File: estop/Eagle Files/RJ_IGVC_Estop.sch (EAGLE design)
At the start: 28 parts, among them U1 LD1086D2M33TR, U4 ATMEGA328P-AUR, X1 2X3SHROUDED, X2 1751248, X3 1751248, X4 1751248, X5 1751248

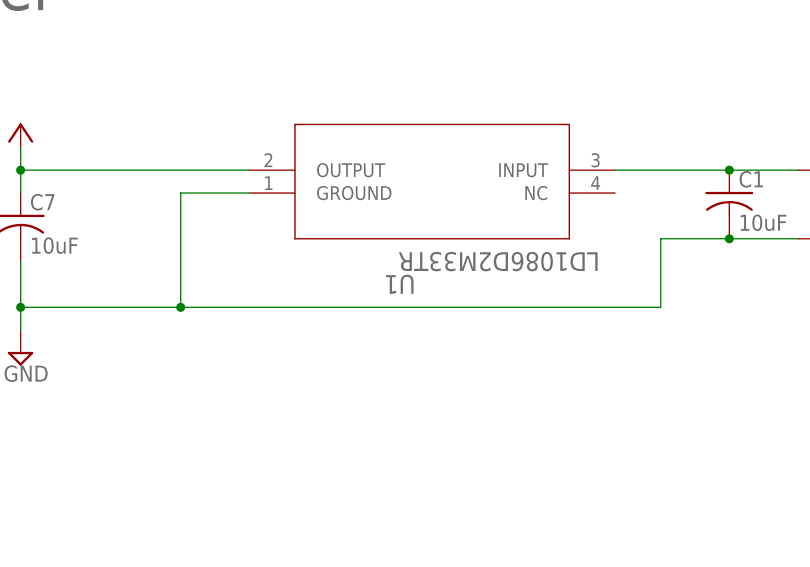
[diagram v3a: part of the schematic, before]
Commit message: Fixed some errors, enlarged some labels, rounded edges
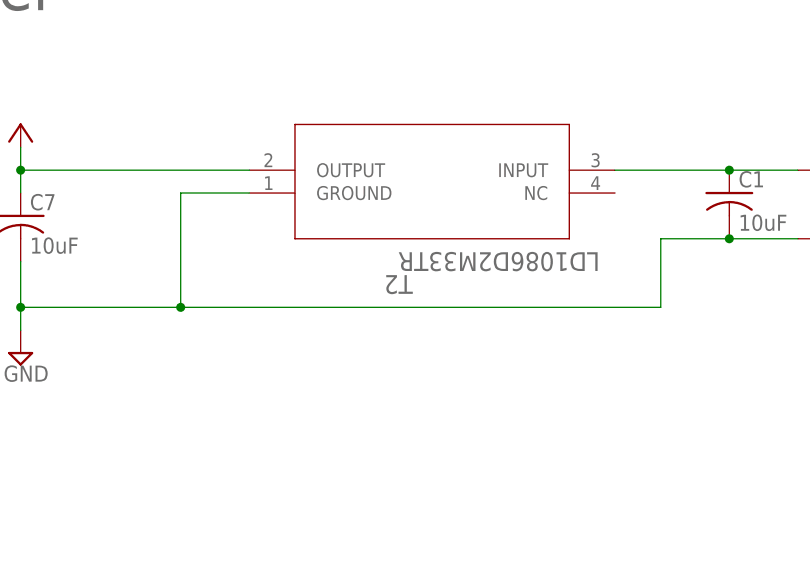
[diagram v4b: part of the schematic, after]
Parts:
- renumbered U$1 to T1, U1 to T2
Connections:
- removed net +3V3: D2.A
- net +3.3V: now also D2.A
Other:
- note removed: "LED"
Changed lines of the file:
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@@
 <part name="R9" library="resistor" library_urn="urn:adsk.eagle:library:348" deviceset="R-US_" device="R0603" package3d_urn="urn:adsk.eagle:package:26057/1" value="4.7k"/>
 <part name="R10" library="resistor" library_urn="urn:adsk.eagle:library:348" deviceset="R-US_" device="R0603" package3d_urn="urn:adsk.eagle:package:26057/1" value="750"/>
-<part name="U$1" library="transistor" deviceset="TRANSISTOR" device=""/>
-<part name="U1" library="transistor" deviceset="LD1086D2M33TR" device=""/>
+<part name="T1" library="transistor" deviceset="TRANSISTOR" device=""/>
+<part name="T2" library="transistor" deviceset="LD1086D2M33TR" device=""/>
 <part name="JP2" library="pinhead" library_urn="urn:adsk.eagle:library:325" deviceset="PINHD-1X3" device="" package3d_urn="urn:adsk.eagle:package:22458/2"/>
 <part name="R3" library="resistor" library_urn="urn:adsk.eagle:library:348" deviceset="R-US_" device="R0603" package3d_urn="urn:adsk.eagle:package:26057/1" value="10k"/>
@@
 <text x="591.82" y="406.4" size="5.08" layer="103" font="vector">24V OUT</text>
 <text x="617.22" y="381" size="1.016" layer="103">Import Symbol</text>
-<text x="345.44" y="271.78" size="1.016" layer="103">LED</text>
 <wire x1="462.28" y1="254" x2="462.28" y2="215.9" width="0.1524" layer="103" style="shortdash"/>
 <wire x1="462.28" y1="215.9" x2="419.1" y2="215.9" width="0.1524" layer="103" style="shortdash"/>
@@
 <instance part="R9" gate="G$1" x="541.02" y="391.16" rot="R270"/>
 <instance part="R10" gate="G$1" x="541.02" y="381" rot="R270"/>
-<instance part="U$1" gate="G$1" x="617.22" y="388.62"/>
-<instance part="U1" gate="A" x="386.08" y="330.2" rot="MR180"/>
+<instance part="T1" gate="G$1" x="617.22" y="388.62"/>
+<instance part="T2" gate="A" x="386.08" y="330.2" rot="MR180"/>
 <instance part="JP2" gate="A" x="403.86" y="251.46"/>
 <instance part="R3" gate="G$1" x="594.36" y="381" rot="R270"/>
@@
 <wire x1="363.22" y1="332.74" x2="363.22" y2="335.28" width="0.1524" layer="91"/>
 <junction x="363.22" y="332.74"/>
-<pinref part="U1" gate="A" pin="OUTPUT"/>
+<pinref part="T2" gate="A" pin="OUTPUT"/>
 <wire x1="363.22" y1="332.74" x2="388.62" y2="332.74" width="0.1524" layer="91"/>
 </segment>
@@
 <wire x1="439.42" y1="396.24" x2="433.07" y2="396.24" width="0.1524" layer="91"/>
 </segment>
+<segment>
+<pinref part="SUPPLY3" gate="G$1" pin="+3V3"/>
+<pinref part="D2" gate="G$1" pin="A"/>
+<wire x1="426.72" y1="281.94" x2="426.72" y2="279.4" width="0.1524" layer="91"/>
+<wire x1="426.72" y1="279.4" x2="431.8" y2="279.4" width="0.1524" layer="91"/>
+</segment>
 </net>
 <net name="GND" class="0">
@@
 <wire x1="434.34" y1="325.12" x2="434.34" y2="317.5" width="0.1524" layer="91"/>
 <wire x1="434.34" y1="317.5" x2="381" y2="317.5" width="0.1524" layer="91"/>
-<pinref part="U1" gate="A" pin="GROUND"/>
+<pinref part="T2" gate="A" pin="GROUND"/>
 <wire x1="388.62" y1="330.2" x2="381" y2="330.2" width="0.1524" layer="91"/>
 <wire x1="381" y1="330.2" x2="381" y2="317.5" width="0.1524" layer="91"/>
@@
 <wire x1="603.25" y1="375.92" x2="603.25" y2="386.08" width="0.1524" layer="91"/>
 <junction x="603.25" y="375.92"/>
-<pinref part="U$1" gate="G$1" pin="S"/>
+<pinref part="T1" gate="G$1" pin="S"/>
 <wire x1="603.25" y1="386.08" x2="609.6" y2="386.08" width="0.1524" layer="91"/>
 </segment>
@@
 <wire x1="429.26" y1="332.74" x2="441.96" y2="332.74" width="0.1524" layer="91"/>
 <junction x="441.96" y="332.74"/>
-<pinref part="U1" gate="A" pin="INPUT"/>
+<pinref part="T2" gate="A" pin="INPUT"/>
 </segment>
 <segment>
@@
 <wire x1="309.88" y1="266.7" x2="307.34" y2="266.7" width="0.1524" layer="91"/>
 <label x="307.34" y="266.7" size="1.27" layer="95" font="vector" rot="MR0" xref="yes"/>
-</segment>
-</net>
-<net name="+3V3" class="0">
-<segment>
-<pinref part="SUPPLY3" gate="G$1" pin="+3V3"/>
-<pinref part="D2" gate="G$1" pin="A"/>
-<wire x1="426.72" y1="281.94" x2="426.72" y2="279.4" width="0.1524" layer="91"/>
-<wire x1="426.72" y1="279.4" x2="431.8" y2="279.4" width="0.1524" layer="91"/>
 </segment>
 </net>
@@
 <segment>
 <label x="594.36" y="398.78" size="1.016" layer="95" font="vector" rot="R90" xref="yes"/>
-<pinref part="U$1" gate="G$1" pin="G"/>
+<pinref part="T1" gate="G$1" pin="G"/>
 <wire x1="594.36" y1="398.78" x2="594.36" y2="388.62" width="0.1524" layer="91"/>
 <pinref part="R3" gate="G$1" pin="1"/>
@@
 <net name="N$1" class="0">
 <segment>
-<pinref part="U$1" gate="G$1" pin="D"/>
+<pinref part="T1" gate="G$1" pin="D"/>
 <pinref part="X5" gate="-2" pin="K"/>
 <wire x1="629.92" y1="388.62" x2="632.46" y2="388.62" width="0.1524" layer="91"/>
